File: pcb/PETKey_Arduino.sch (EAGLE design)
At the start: 6 parts, among them X2 KB_PORT_PET

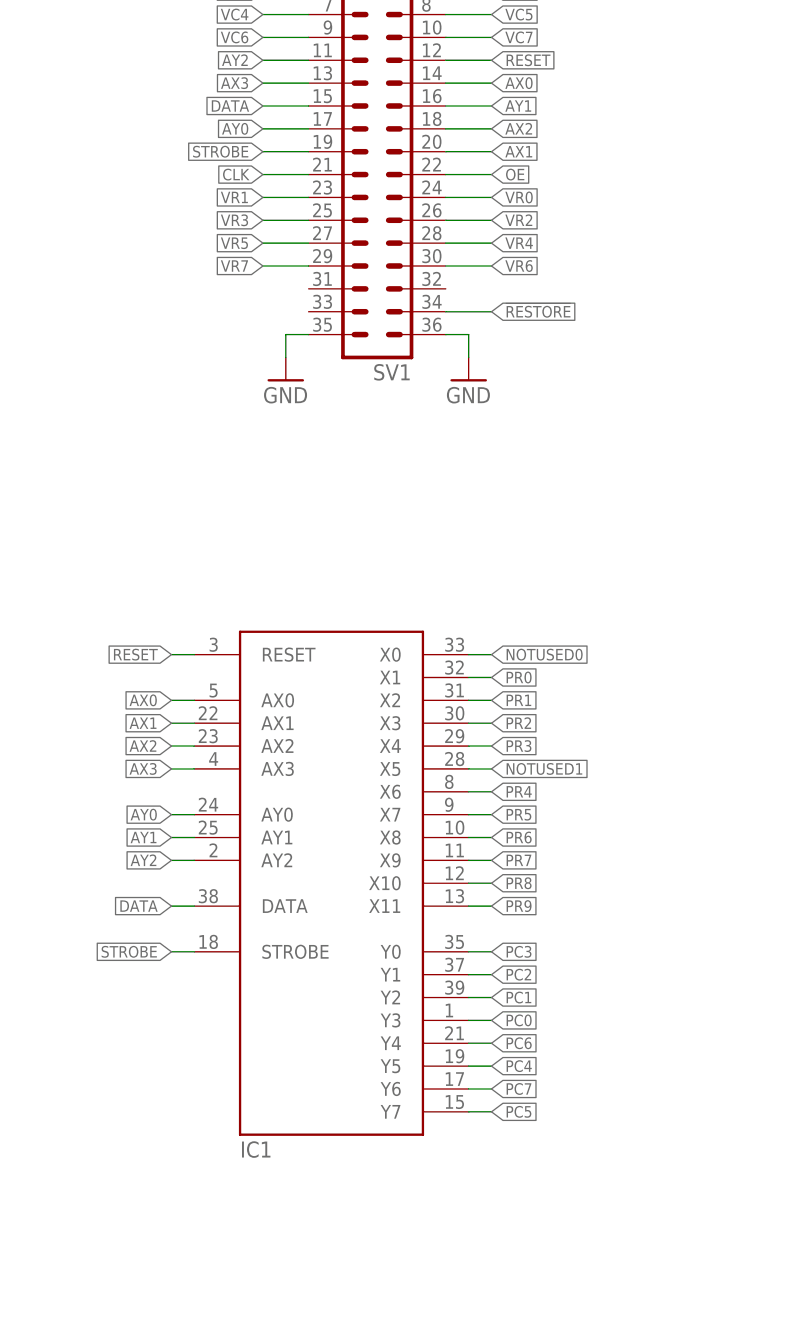
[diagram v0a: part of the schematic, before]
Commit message: Fix incorrect XPT mappings
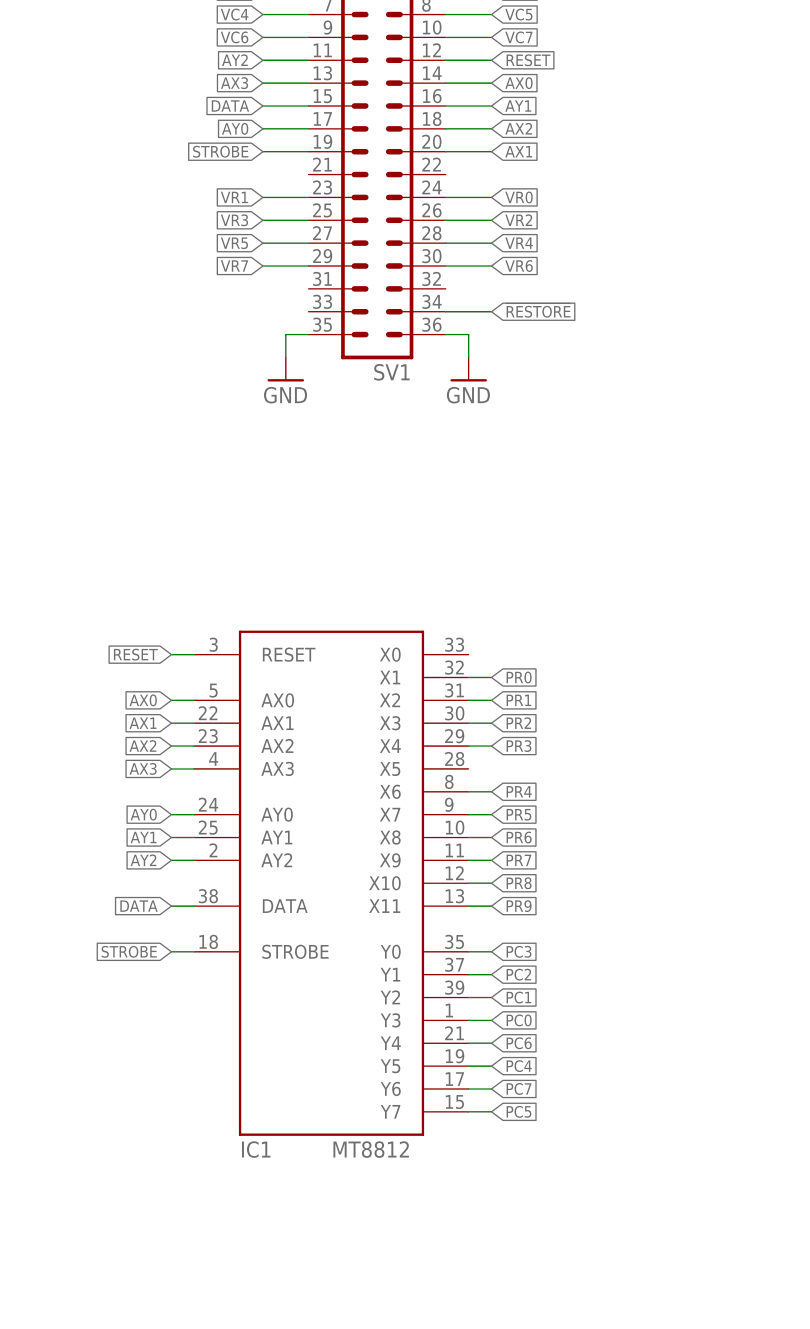
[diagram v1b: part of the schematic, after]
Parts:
- IC1: value (none) -> MT8812
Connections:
- removed net CLK: SV1.21
- removed net NOTUSED0: IC1A.X0
- removed net NOTUSED1: IC1A.X5
- removed net OE: SV1.22
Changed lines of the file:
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@@
 <part name="GOLD_ORB_SM1" library="oshw" deviceset="OSHWLOGO" device="LOGO8MM" value="Open Source Hardware"/>
 <part name="X1" library="commodore" deviceset="KB_PORT_VIC/64" device=""/>
-<part name="IC1" library="MT8812" deviceset="MT8812" device=""/>
+<part name="IC1" library="MT8812" deviceset="MT8812" device="" value="MT8812"/>
 <part name="GND1" library="supply1" deviceset="GND" device=""/>
 <part name="X2" library="commodore" deviceset="KB_PORT_PET" device=""/>
@@
 </busses>
 <nets>
-<net name="CLK" class="0">
-<segment>
-<pinref part="SV1" gate="G$1" pin="21"/>
-<wire x1="152.4" y1="167.64" x2="147.32" y2="167.64" width="0.1524" layer="91"/>
-<label x="147.32" y="167.64" size="1.27" layer="95" ratio="10" rot="R180" xref="yes"/>
-</segment>
-</net>
-<net name="OE" class="0">
-<segment>
-<pinref part="SV1" gate="G$1" pin="22"/>
-<wire x1="167.64" y1="167.64" x2="172.72" y2="167.64" width="0.1524" layer="91"/>
-<label x="172.72" y="167.64" size="1.27" layer="95" ratio="10" xref="yes"/>
-</segment>
-</net>
 <net name="VCC" class="0">
 <segment>
@@
 </segment>
 </net>
-<net name="NOTUSED0" class="0">
-<segment>
-<pinref part="IC1" gate="A" pin="X0"/>
-<wire x1="170.18" y1="114.3" x2="172.72" y2="114.3" width="0.1524" layer="91"/>
-<label x="172.72" y="114.3" size="1.27" layer="95" ratio="10" xref="yes"/>
-</segment>
-</net>
-<net name="NOTUSED1" class="0">
-<segment>
-<pinref part="IC1" gate="A" pin="X5"/>
-<wire x1="170.18" y1="101.6" x2="172.72" y2="101.6" width="0.1524" layer="91"/>
-<label x="172.72" y="101.6" size="1.27" layer="95" ratio="10" xref="yes"/>
-</segment>
-</net>
